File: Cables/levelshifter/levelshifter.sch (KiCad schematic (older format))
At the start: 56 parts, among them J1 DB25_Male, J10 Conn_01x01, J11 Conn_01x01, J12 Conn_01x01, J13 Conn_01x01, J14 Conn_01x01, J15 Conn_01x01, J16 Conn_01x01, J17 Conn_01x01, J19 Conn_01x01, J2 Conn_01x01, J20 Conn_01x01, J21 Conn_01x01, J22 Conn_01x01, J23 Conn_01x01, J24 Conn_01x01, J25 Conn_01x01, J26 Conn_01x01, J27 Conn_01x01, J28 Conn_01x01, J29 Conn_01x01, J3 Conn_01x01, J4 Conn_01x01, J5 Conn_01x01, J6 Conn_01x01, J7 Conn_01x01, J9 Conn_01x01, U1 74AHCT1G126, U10 74AHCT1G125, U11 74AHCT1G125, U12 74AHCT1G125, U13 74AHCT1G125, U14 74AHCT1G126, U15 74AHCT1G126, U16 74AHCT1G126, U17 74AHCT1G126, U18 74AHCT1G126, U19 74AHCT1G126, U2 74AHCT1G126, U20 74AHCT1G126, U21 74AHCT1G125, U22 74AHCT1G125, U23 74AHCT1G125, U24 74AHCT1G125, U25 74AHCT1G125, U26 74AHCT1G125, U27 74AHCT1G126, U28 74AHCT1G125, U3 74AHCT1G126, U4 74AHCT1G126, U5 74AHCT1G126, U6 74AHCT1G126, U7 74AHCT1G126, U8 74AHCT1G125, U9 74AHCT1G125

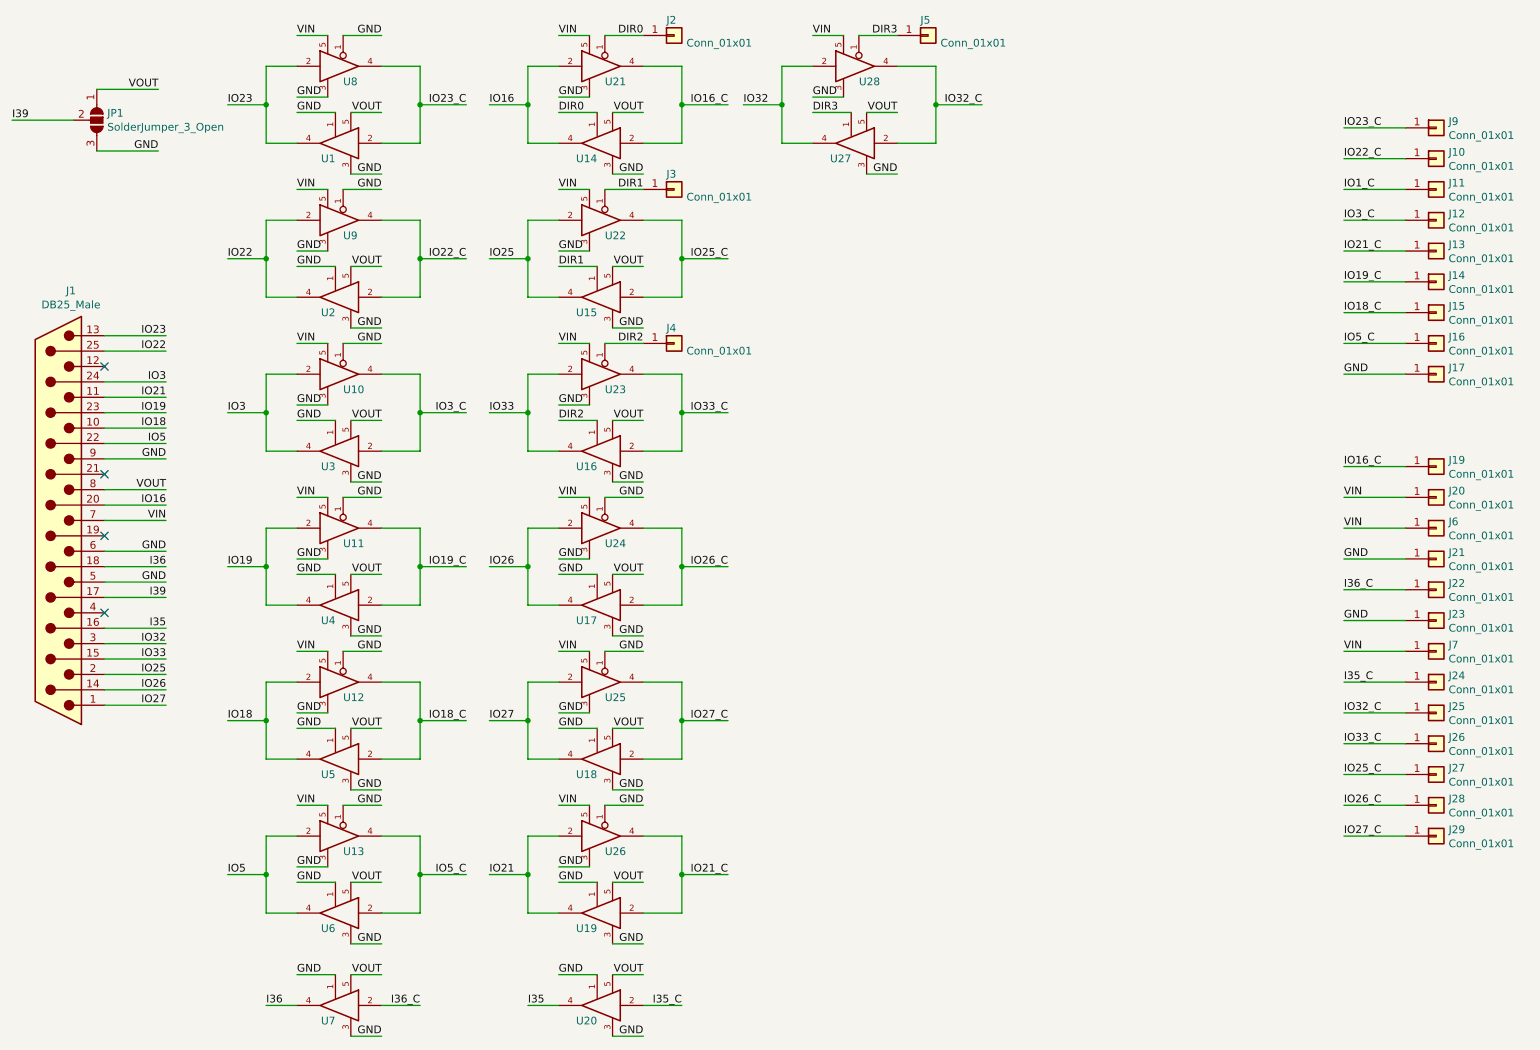
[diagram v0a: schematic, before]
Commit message: Fixup inverted DB25 for Level Shifter PCB
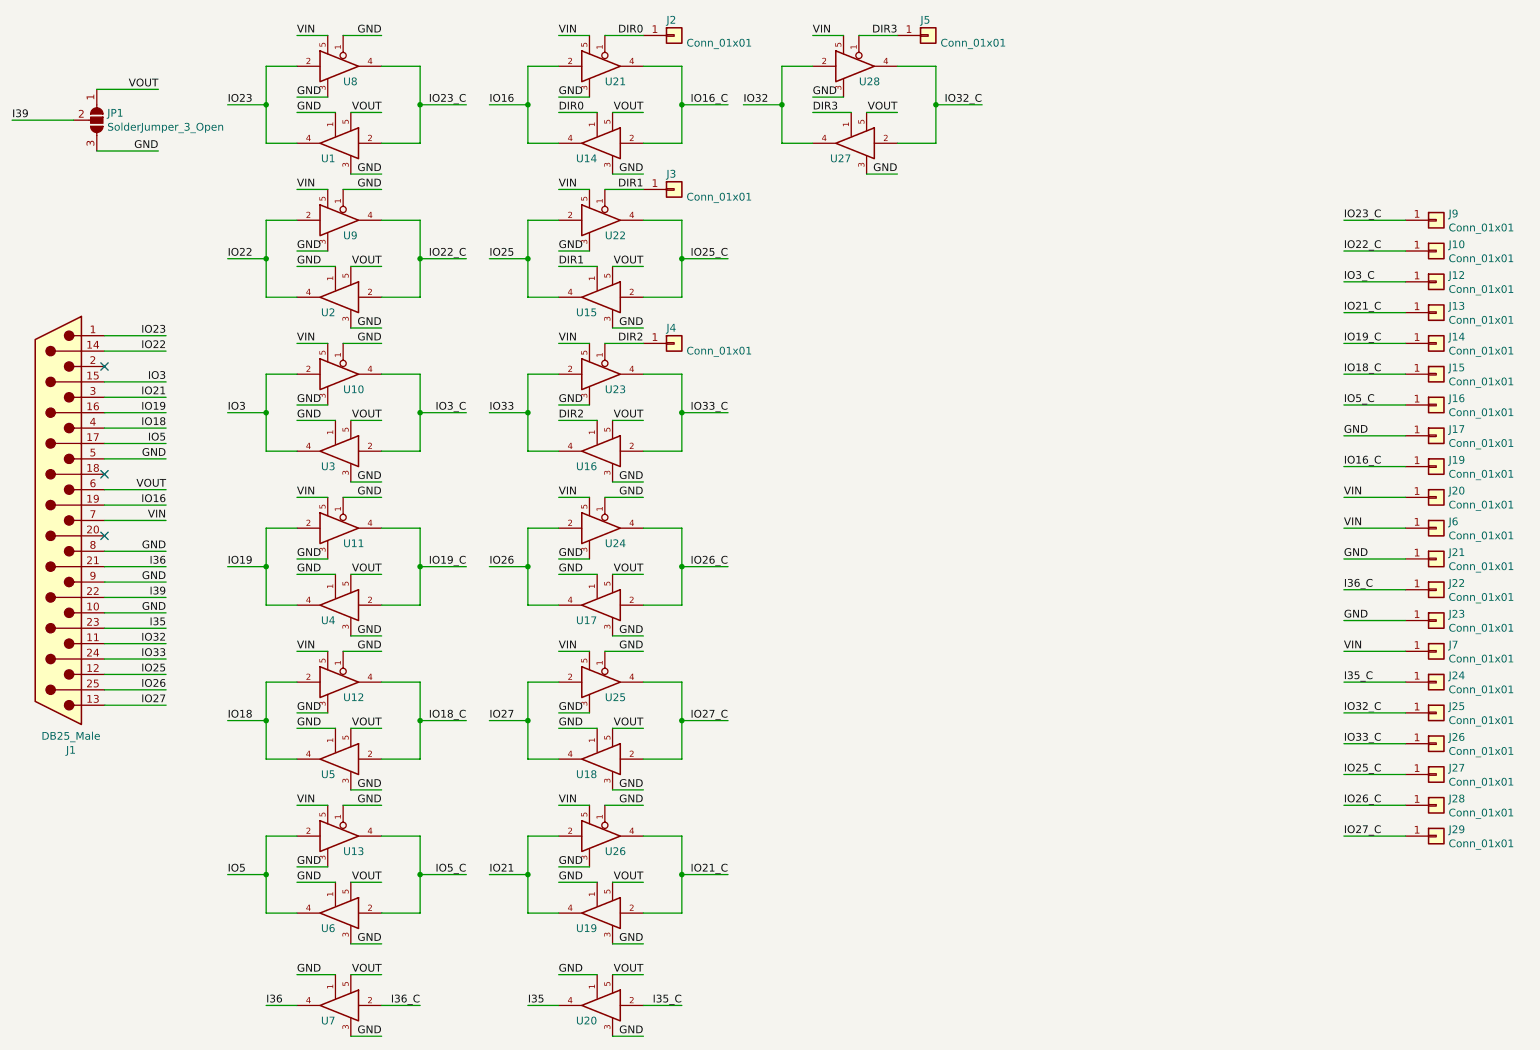
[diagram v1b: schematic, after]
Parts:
- removed J11: Conn_01x01, levelshifter:SolderWirePad_1x01_SMD_1x2mm, symbol levelshifter:Conn_01x01
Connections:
- net GND: now also J1.10, J1.8; no longer J1.6
- net I35: now also J1.23 (P23); no longer J1.16 (P16)
- net I36: now also J1.21 (P21); no longer J1.18 (P18)
- net I39: now also J1.22 (P22); no longer J1.17 (P17)
- net IO16: now also J1.19 (P19); no longer J1.20 (P20)
- net IO18: now also J1.4; no longer J1.10
- net IO19: now also J1.16 (P16); no longer J1.23 (P23)
- net IO21: now also J1.3; no longer J1.11
- net IO22: now also J1.14 (P14); no longer J1.25 (P25)
- net IO23: now also J1.1; no longer J1.13
- net IO25: now also J1.12; no longer J1.2
- net IO26: now also J1.25 (P25); no longer J1.14 (P14)
- net IO27: now also J1.13; no longer J1.1
- net IO3: now also J1.15 (P15); no longer J1.24 (P24)
- net IO32: now also J1.11; no longer J1.3
- net IO33: now also J1.24 (P24); no longer J1.15 (P15)
- net IO5: now also J1.17 (P17); no longer J1.22 (P22)
- net VOUT: now also J1.6; no longer J1.8
- no-connect marks 4 -> 3
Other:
- moved on the sheet: J10, J12, J13, J14, J15, J16, J17, J9
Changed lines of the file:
@@
 Sheet 1 1
 Title "BlueRetro - Level shifter cable adapter (5V)"
-Date "2020-09-02"
-Rev "v1.0"
+Date "2020-09-06"
+Rev "v1.1"
 Comp ""
 Comment1 ""
@@
 F 3 " ~" H 900 3800 50  0001 C CNN
 	1    900  3800
-	-1   0    0    -1
+	-1   0    0    1
 $EndComp
 $Comp
 L levelshifter:Conn_01x01 J9
 U 1 1 5F4421F4
-P 9850 1250
-F 0 "J9" H 9930 1292 50  0000 L CNN
-F 1 "Conn_01x01" H 9930 1201 50  0000 L CNN
-F 2 "levelshifter:SolderWirePad_1x01_SMD_1x2mm" H 9850 1250 50  0001 C CNN
-F 3 "~" H 9850 1250 50  0001 C CNN
-	1    9850 1250
-	1    0    0    -1
-$EndComp
-$Comp
-L levelshifter:Conn_01x01 J10
-U 1 1 5F4454D6
-P 9850 1450
-F 0 "J10" H 9930 1492 50  0000 L CNN
-F 1 "Conn_01x01" H 9930 1401 50  0000 L CNN
-F 2 "levelshifter:SolderWirePad_1x01_SMD_1x2mm" H 9850 1450 50  0001 C CNN
-F 3 "~" H 9850 1450 50  0001 C CNN
-	1    9850 1450
-	1    0    0    -1
-$EndComp
-$Comp
-L levelshifter:Conn_01x01 J12
-U 1 1 5F4457E0
 P 9850 1850
-F 0 "J12" H 9930 1892 50  0000 L CNN
+F 0 "J9" H 9930 1892 50  0000 L CNN
 F 1 "Conn_01x01" H 9930 1801 50  0000 L CNN
 F 2 "levelshifter:SolderWirePad_1x01_SMD_1x2mm" H 9850 1850 50  0001 C CNN
@@
 $EndComp
 $Comp
-L levelshifter:Conn_01x01 J14
-U 1 1 5F44597F
+L levelshifter:Conn_01x01 J10
+U 1 1 5F4454D6
+P 9850 2050
+F 0 "J10" H 9930 2092 50  0000 L CNN
+F 1 "Conn_01x01" H 9930 2001 50  0000 L CNN
+F 2 "levelshifter:SolderWirePad_1x01_SMD_1x2mm" H 9850 2050 50  0001 C CNN
+F 3 "~" H 9850 2050 50  0001 C CNN
+	1    9850 2050
+	1    0    0    -1
+$EndComp
+$Comp
+L levelshifter:Conn_01x01 J12
+U 1 1 5F4457E0
 P 9850 2250
-F 0 "J14" H 9930 2292 50  0000 L CNN
+F 0 "J12" H 9930 2292 50  0000 L CNN
 F 1 "Conn_01x01" H 9930 2201 50  0000 L CNN
 F 2 "levelshifter:SolderWirePad_1x01_SMD_1x2mm" H 9850 2250 50  0001 C CNN
@@
 $EndComp
 $Comp
-L levelshifter:Conn_01x01 J16
-U 1 1 5F445B44
+L levelshifter:Conn_01x01 J14
+U 1 1 5F44597F
 P 9850 2650
-F 0 "J16" H 9930 2692 50  0000 L CNN
+F 0 "J14" H 9930 2692 50  0000 L CNN
 F 1 "Conn_01x01" H 9930 2601 50  0000 L CNN
 F 2 "levelshifter:SolderWirePad_1x01_SMD_1x2mm" H 9850 2650 50  0001 C CNN
@@
 $EndComp
 $Comp
+L levelshifter:Conn_01x01 J16
+U 1 1 5F445B44
+P 9850 3050
+F 0 "J16" H 9930 3092 50  0000 L CNN
+F 1 "Conn_01x01" H 9930 3001 50  0000 L CNN
+F 2 "levelshifter:SolderWirePad_1x01_SMD_1x2mm" H 9850 3050 50  0001 C CNN
+F 3 "~" H 9850 3050 50  0001 C CNN
+	1    9850 3050
+	1    0    0    -1
+$EndComp
+$Comp
 L levelshifter:Conn_01x01 J17
 U 1 1 5F445CF5
-P 9850 2850
-F 0 "J17" H 9930 2892 50  0000 L CNN
-F 1 "Conn_01x01" H 9930 2801 50  0000 L CNN
-F 2 "levelshifter:SolderWirePad_1x01_SMD_1x2mm" H 9850 2850 50  0001 C CNN
-F 3 "~" H 9850 2850 50  0001 C CNN
-	1    9850 2850
+P 9850 3250
+F 0 "J17" H 9930 3292 50  0000 L CNN
+F 1 "Conn_01x01" H 9930 3201 50  0000 L CNN
+F 2 "levelshifter:SolderWirePad_1x01_SMD_1x2mm" H 9850 3250 50  0001 C CNN
+F 3 "~" H 9850 3250 50  0001 C CNN
+	1    9850 3250
 	1    0    0    -1
 $EndComp
@@
 L levelshifter:Conn_01x01 J13
 U 1 1 5F446F73
-P 9850 2050
-F 0 "J13" H 9930 2092 50  0000 L CNN
-F 1 "Conn_01x01" H 9930 2001 50  0000 L CNN
-F 2 "levelshifter:SolderWirePad_1x01_SMD_1x2mm" H 9850 2050 50  0001 C CNN
-F 3 "~" H 9850 2050 50  0001 C CNN
-	1    9850 2050
-	1    0    0    -1
-$EndComp
-$Comp
-L levelshifter:Conn_01x01 J15
-U 1 1 5F447330
 P 9850 2450
-F 0 "J15" H 9930 2492 50  0000 L CNN
+F 0 "J13" H 9930 2492 50  0000 L CNN
 F 1 "Conn_01x01" H 9930 2401 50  0000 L CNN
 F 2 "levelshifter:SolderWirePad_1x01_SMD_1x2mm" H 9850 2450 50  0001 C CNN
 F 3 "~" H 9850 2450 50  0001 C CNN
 	1    9850 2450
+	1    0    0    -1
+$EndComp
+$Comp
+L levelshifter:Conn_01x01 J15
+U 1 1 5F447330
+P 9850 2850
+F 0 "J15" H 9930 2892 50  0000 L CNN
+F 1 "Conn_01x01" H 9930 2801 50  0000 L CNN
+F 2 "levelshifter:SolderWirePad_1x01_SMD_1x2mm" H 9850 2850 50  0001 C CNN
+F 3 "~" H 9850 2850 50  0001 C CNN
+	1    9850 2850
 	1    0    0    -1
 $EndComp
@@
 	1200 5000 1600 5000
 Wire Wire Line
-	9650 1250 9250 1250
-Wire Wire Line
-	9650 1450 9250 1450
-Wire Wire Line
 	9650 1850 9250 1850
 Wire Wire Line
@@
 Wire Wire Line
 	9650 2850 9250 2850
+Wire Wire Line
+	9650 3050 9250 3050
+Wire Wire Line
+	9650 3250 9250 3250
 Wire Wire Line
 	9650 3450 9250 3450
@@
 Wire Wire Line
 	9650 5850 9250 5850
-Text Label 9250 1250 0    50   ~ 0
+Text Label 9250 1850 0    50   ~ 0
 IO23_C
-Text Label 9250 1450 0    50   ~ 0
+Text Label 9250 2050 0    50   ~ 0
 IO22_C
-Text Label 9250 1850 0    50   ~ 0
+Text Label 9250 2250 0    50   ~ 0
 IO3_C
-Text Label 9250 2050 0    50   ~ 0
+Text Label 9250 2450 0    50   ~ 0
 IO21_C
-Text Label 9250 2250 0    50   ~ 0
+Text Label 9250 2650 0    50   ~ 0
 IO19_C
-Text Label 9250 2450 0    50   ~ 0
+Text Label 9250 2850 0    50   ~ 0
 IO18_C
-Text Label 9250 2650 0    50   ~ 0
+Text Label 9250 3050 0    50   ~ 0
 IO5_C
-Text Label 9250 2850 0    50   ~ 0
+Text Label 9250 3250 0    50   ~ 0
 GND
 Text Label 9250 3450 0    50   ~ 0
@@
 Text Label 1550 1400 2    50   ~ 0
 GND
-Wire Wire Line
-	9650 1650 9250 1650
-$Comp
-L levelshifter:Conn_01x01 J11
-U 1 1 5F445672
-P 9850 1650
-F 0 "J11" H 9930 1692 50  0000 L CNN
-F 1 "Conn_01x01" H 9930 1601 50  0000 L CNN
-F 2 "levelshifter:SolderWirePad_1x01_SMD_1x2mm" H 9850 1650 50  0001 C CNN
-F 3 "~" H 9850 1650 50  0001 C CNN
-	1    9850 1650
-	1    0    0    -1
-$EndComp
-Text Label 9250 1650 0    50   ~ 0
-IO1_C
 NoConn ~ 1200 3500
 NoConn ~ 1200 3900
-NoConn ~ 1200 4400
 $Comp
 L levelshifter:74AHCT1G125 U8
@@
 Text Label 9250 4650 0    50   ~ 0
 VIN
+Wire Wire Line
+	1200 4400 1600 4400
+Text Label 1600 4400 2    50   ~ 0
+GND
 $EndSCHEMATC

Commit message: Final tweak for JVS & LS PCBs
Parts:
- added J8: Conn_01x01, levelshifter:SolderWirePad_1x01_SMD_1x2mm, symbol levelshifter:Conn_01x01
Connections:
- net GND: no longer U18.1, U25.1
- new net DIR4: J8.1 (Pin_1), U18.1, U25.1
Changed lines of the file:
@@
 	4500 5550 4700 5550
 Text Label 4150 5150 0    50   ~ 0
-GND
+DIR4
 Text Label 4700 5150 2    50   ~ 0
 VOUT
@@
 Wire Wire Line
 	4450 4650 4700 4650
-Text Label 4700 4650 2    50   ~ 0
-GND
 Text Label 4150 4650 0    50   ~ 0
 VIN
@@
 Text Label 1600 4400 2    50   ~ 0
 GND
+$Comp
+L levelshifter:Conn_01x01 J8
+U 1 1 5F58DF76
+P 4900 4650
+F 0 "J8" H 4850 4750 50  0000 L CNN
+F 1 "Conn_01x01" H 4980 4601 50  0000 L CNN
+F 2 "levelshifter:SolderWirePad_1x01_SMD_1x2mm" H 4900 4650 50  0001 C CNN
+F 3 "~" H 4900 4650 50  0001 C CNN
+	1    4900 4650
+	1    0    0    -1
+$EndComp
+Text Label 4700 4650 2    50   ~ 0
+DIR4
 $EndSCHEMATC

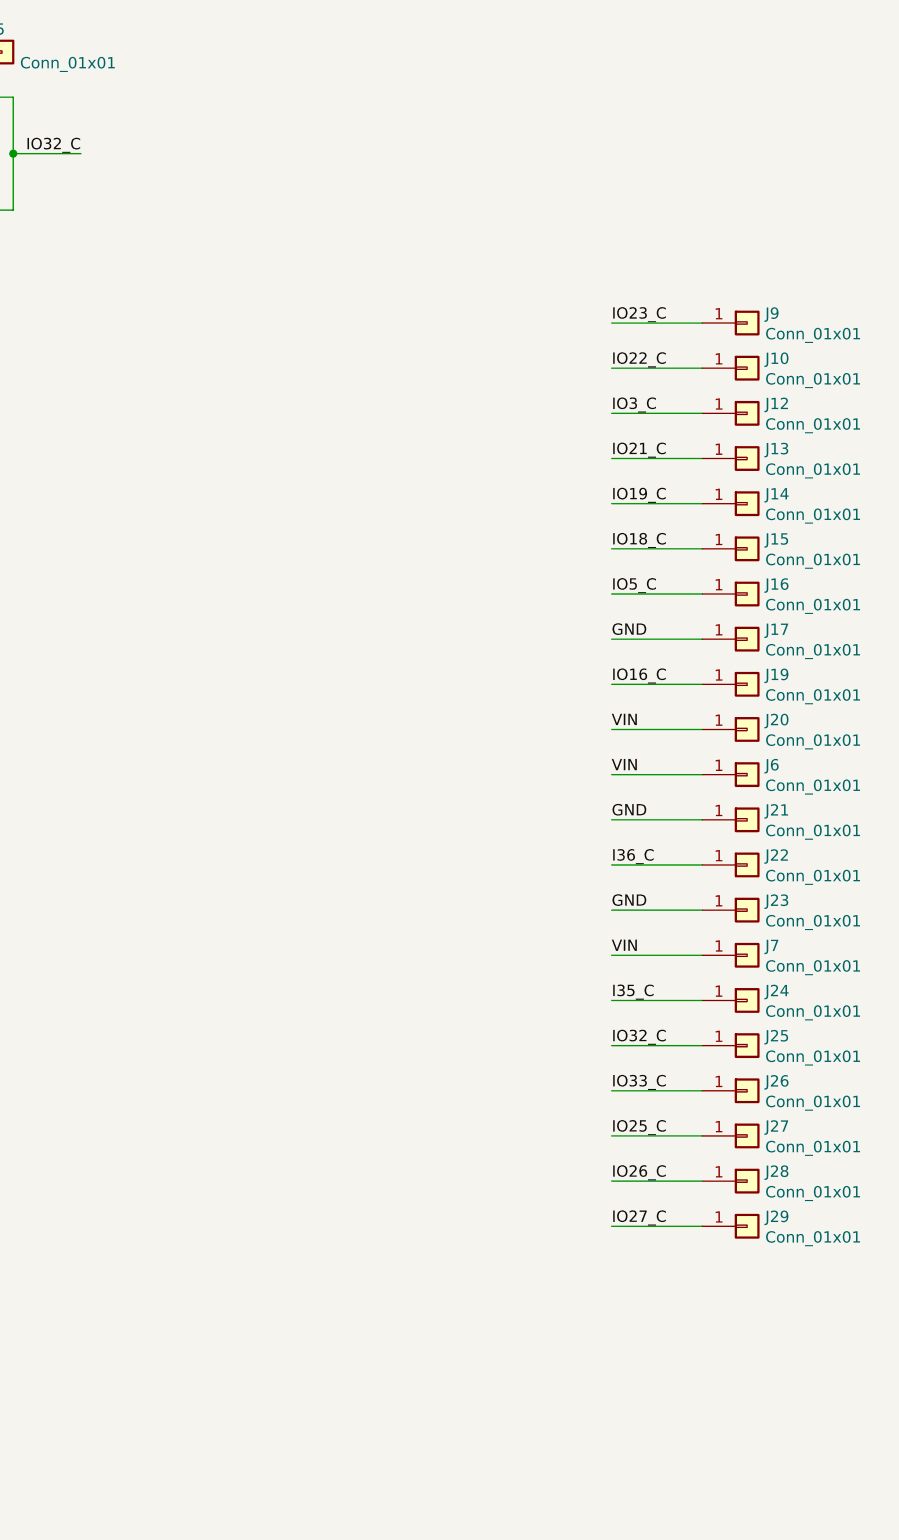
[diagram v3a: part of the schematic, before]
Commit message: [LS] Add pull-up footprint on 5V side for PAL NES & SNES cables
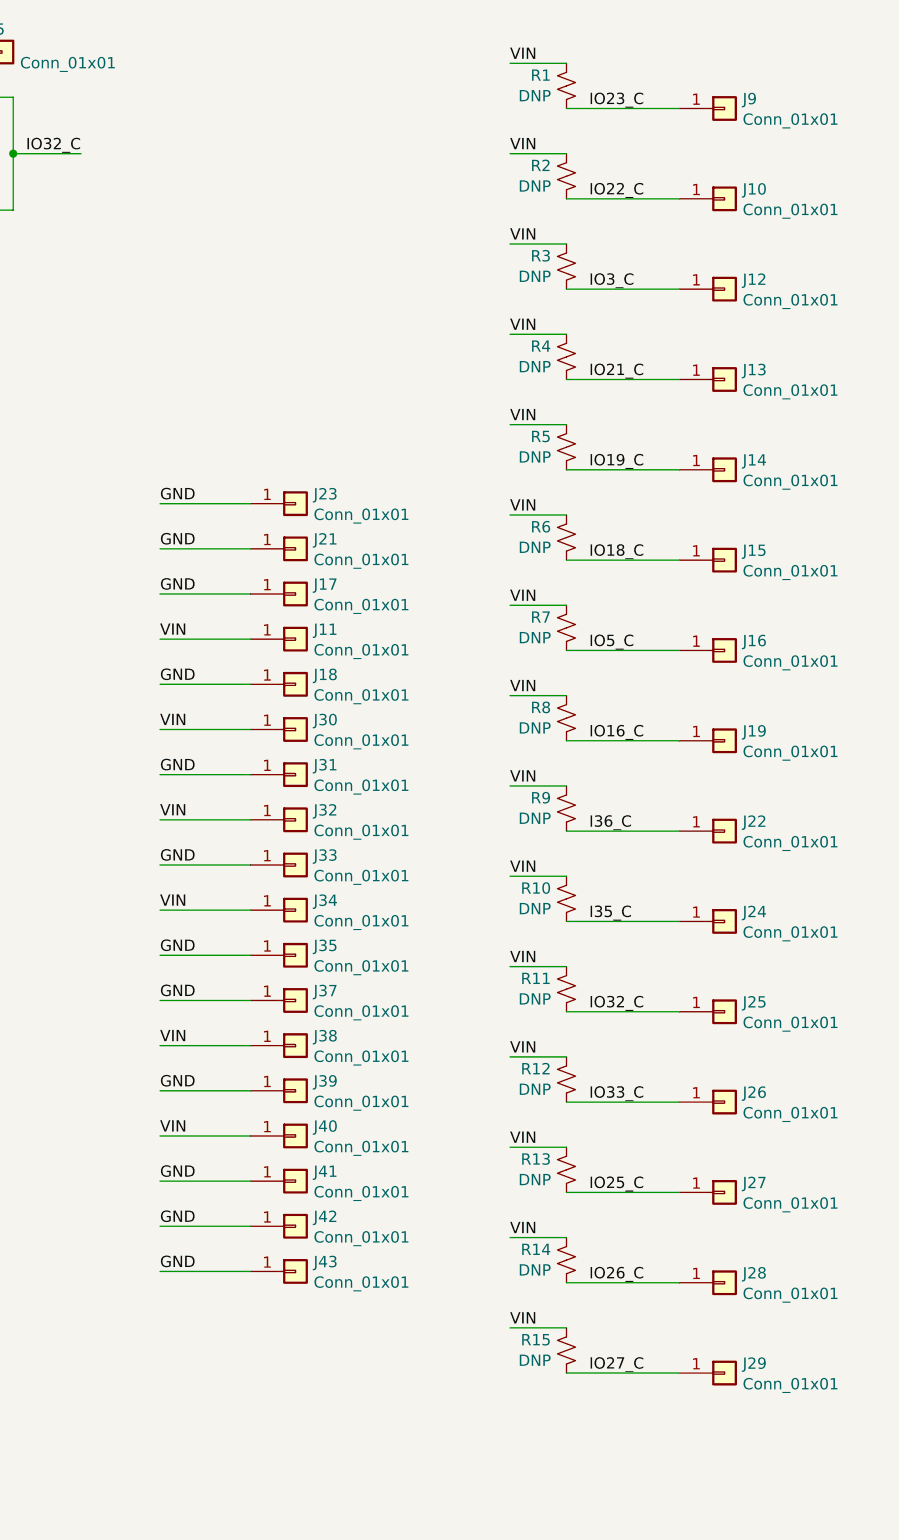
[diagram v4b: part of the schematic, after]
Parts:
- removed J20, J6, J7: Conn_01x01, levelshifter:SolderWirePad_1x01_SMD_1x2mm, symbol levelshifter:Conn_01x01
- added J11, J18, J30, J31, J32, J33, J34, J35, J37, J38, J39, J40, J41, J42, J43: Conn_01x01, levelshifter:SolderWirePad_1x01_SMD_1x2mm, symbol levelshifter:Conn_01x01
- added R1, R10, R11, R12, R13, R14, R15, R2, R3, R4, R5, R6, R7, R8, R9: DNP, levelshifter:R_0402_1005Metric, symbol levelshifter:R_Small_US
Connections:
- net GND: now also J18.1 (Pin_1), J31.1 (Pin_1), J33.1 (Pin_1), J35.1 (Pin_1), J37.1 (Pin_1), J39.1 (Pin_1), J41.1 (Pin_1), J42.1 (Pin_1), J43.1 (Pin_1)
- net I35_C: now also R10.2
- net I36_C: now also R9.2
- net IO16_C: now also R8.2
- net IO18_C: now also R6.2
- net IO19_C: now also R5.2
- net IO21_C: now also R4.2
- net IO22_C: now also R2.2
- net IO23_C: now also R1.2
- net IO25_C: now also R13.2
- net IO26_C: now also R14.2
- net IO27_C: now also R15.2
- net IO32_C: now also R11.2
- net IO33_C: now also R12.2
- net IO3_C: now also R3.2
- net IO5_C: now also R7.2
- net VIN: now also J11.1 (Pin_1), J30.1 (Pin_1), J32.1 (Pin_1), J34.1 (Pin_1), J38.1 (Pin_1), J40.1 (Pin_1), R1.1, R10.1, R11.1, R12.1, R13.1, R14.1, R15.1, R2.1, R3.1, R4.1, R5.1, R6.1, R7.1, R8.1, R9.1
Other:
- moved on the sheet: J10, J12, J13, J14, J15, J16, J17, J19, J21, J22, J23, J24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
